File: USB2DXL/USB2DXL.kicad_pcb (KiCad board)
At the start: 4 copper layers, 38 x 42 mm, 43 parts, among them J1 XT60, J2 USB_C_Receptacle_USB2.0_16P, J3 Conn_01x03, J4 Conn_01x04, J5 Conn_01x03, J6 Conn_01x04, J7 Conn_01x04, U1 CH340E, U2 ISO7741DWR, U3 78L05G-AB3-R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

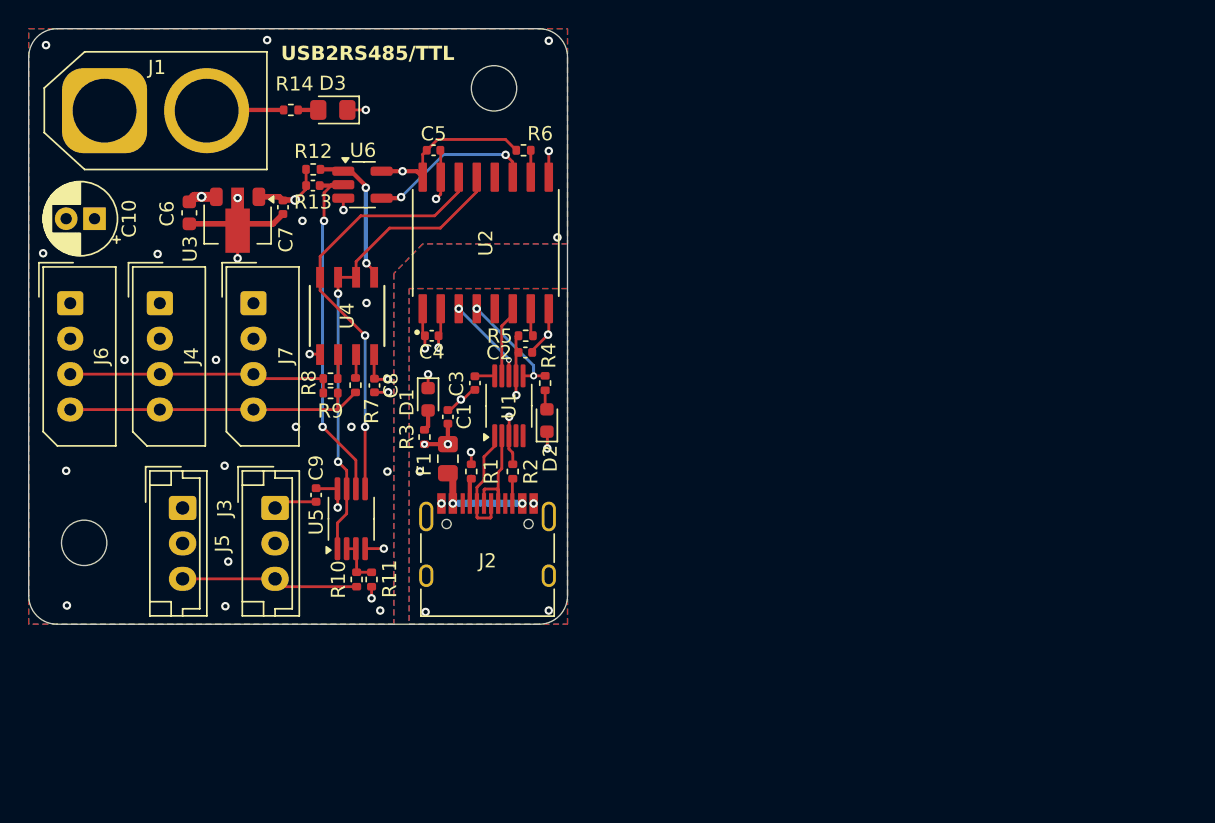
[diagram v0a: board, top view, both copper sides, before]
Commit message: マイコンからのUARTで動かせるようにした
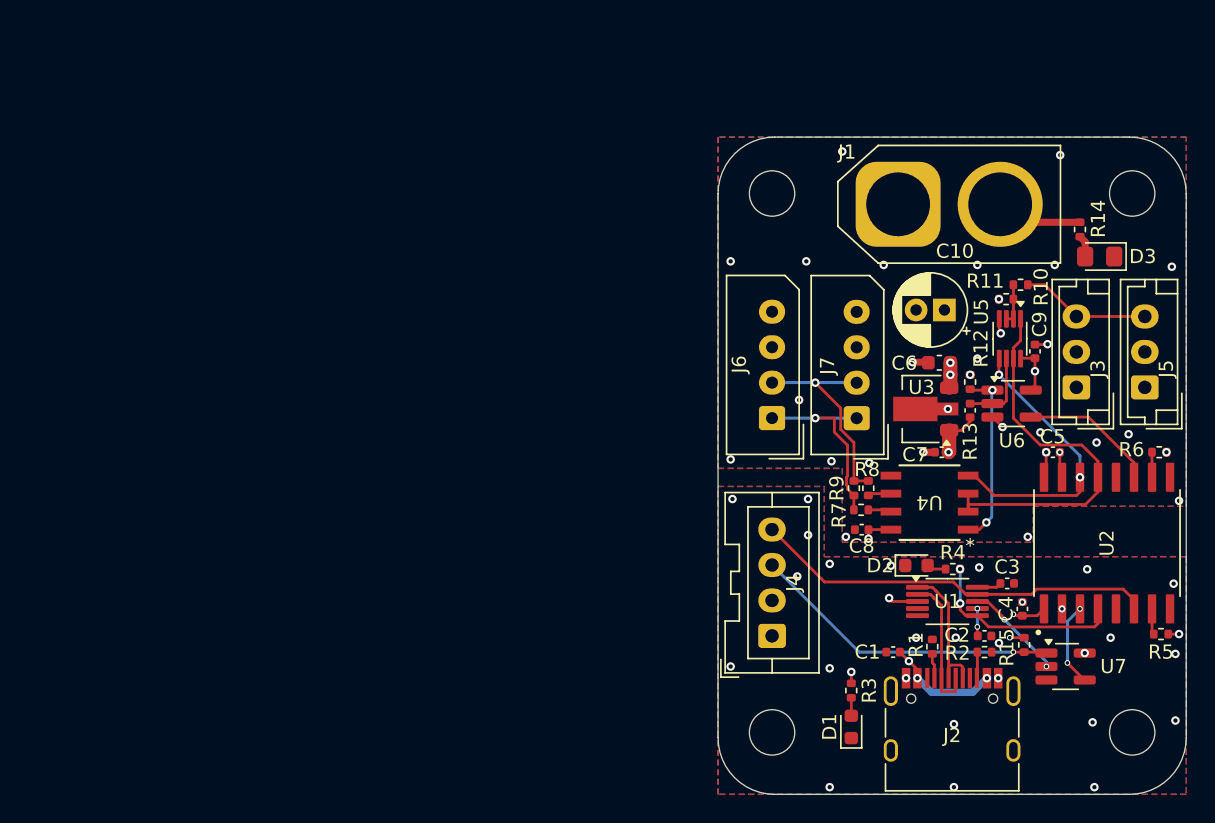
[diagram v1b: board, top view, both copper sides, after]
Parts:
- removed F1: Resettable Fuse, Fuse:Fuse_0805_2012Metric_Pad1.15x1.40mm_HandSolder
- removed the REF** at (54.4, 88.6)
- removed the REF** at (83.3, 56.6)
- added R15: 10k, Resistor_SMD:R_0402_1005Metric, F.Cu at (120.7, 95.8)
- added REF**: MountingHole_3.2mm_M3, MountingHole:MountingHole_3.2mm_M3, F.Cu at (102.9, 64.0)
- added REF**: MountingHole_3.2mm_M3, MountingHole:MountingHole_3.2mm_M3, F.Cu at (128.3, 64.0)
- added REF**: MountingHole_3.2mm_M3, MountingHole:MountingHole_3.2mm_M3, F.Cu at (102.9, 102.0)
- added REF**: MountingHole_3.2mm_M3, MountingHole:MountingHole_3.2mm_M3, F.Cu at (128.3, 102.0)
- added U7: 74AHC1G08, Package_TO_SOT_SMD:SOT-23-5_HandSoldering, F.Cu at (123.6, 97.4)
- J4: footprint Connector_Molex:Molex_SPOX_5267-04A_1x04_P2.50mm_Vertical -> Connector_JST:JST_XA_B04B-XASK-1_1x04_P2.50mm_Vertical
- R4: value 470 -> 1k
- U5: footprint Package_SO:MSOP-8_3x3mm_P0.65mm -> Package_SO:VSSOP-8_2.3x2mm_P0.5mm
- moved J5 68.4 mm to (129.2, 77.7), turned to 90 degrees
- moved C10 60.3 mm to (115.0, 72.2)
- moved J3 57.2 mm to (124.3, 77.7), turned to 90 degrees
- moved J1 56.4 mm to (111.8, 64.8)
- moved R14 56.3 mm to (124.6, 66.5), turned to -90 degrees
- moved D3 55.1 mm to (126.0, 68.5)
- moved C6 53.9 mm to (114.7, 75.9), turned to 180 degrees
- moved C9 51.7 mm to (121.4, 75.1), turned to 90 degrees
- moved R10 51.2 mm to (120.4, 70.4), turned to 0 degrees
- moved J6 50.2 mm to (102.9, 79.8), turned to 90 degrees
- moved U3 50.0 mm to (113.4, 79.2), turned to 180 degrees
- moved R6 49.6 mm to (130.2, 82.3), turned to 0 degrees
- moved C7 49.6 mm to (114.8, 82.3), turned to 180 degrees
- moved R5 49.5 mm to (130.3, 95.1), turned to 180 degrees
- moved J4 49.1 mm to (102.9, 95.2), turned to 90 degrees
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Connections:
- J2 pad A4: Net-(F1-Pad1) -> +5V
- J2 pad A6: /D- -> /D+
- J2 pad A7: /D+ -> /D-
- J2 pad A9: Net-(F1-Pad1) -> +5V
- J2 pad B4: Net-(F1-Pad1) -> +5V
- J2 pad B6: /D- -> /D+
- J2 pad B7: /D+ -> /D-
- J2 pad B9: Net-(F1-Pad1) -> +5V
- J4 pad 1: GNDPWR -> GND
- J4 pad 2: +12V -> +5V
- J4 pad 3: /A -> /TX_pin
- J4 pad 4: /B -> /RXD
- J6 pad 1: GNDPWR -> /DATA-
- J6 pad 2: +12V -> /DATA+
- J6 pad 3: /A -> +12V
- J6 pad 4: /B -> GNDPWR
- J7 pad 1: GNDPWR -> /DATA-
- J7 pad 2: +12V -> /DATA+
- J7 pad 3: /A -> +12V
- J7 pad 4: /B -> GNDPWR
- R7 pad 2: /B -> /DATA-
- R8 pad 2: /A -> /DATA+
- R9 pad 1: /A -> /DATA+
- R9 pad 2: /B -> /DATA-
- U1 pad 8: /TXD -> /TX_usb
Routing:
- net +5VP: track 23.4 -> 54.9 mm, vias 5 -> 7
- net /RXD: track 5.05 -> 28.5 mm
- net /TX_pin: track 0.00 -> 21.9 mm, vias 0 -> 1
- net /B: track 21.8 -> 0.00 mm
- net Net-(U5-Y1): track 25.2 -> 5.61 mm, vias 2 -> 0
- net /A: track 19.0 -> 0.00 mm
- net GNDPWR: track 24.8 -> 6.76 mm, vias 28 -> 26
- net /DATA+: track 0.00 -> 15.1 mm, vias 0 -> 1
- net /DATA-: track 0.00 -> 14.4 mm, vias 0 -> 1
- net GND: track 15.2 -> 2.10 mm, vias 12 -> 27
- net /TX: track 30.4 -> 20.3 mm
- net Net-(F1-Pad1): track 7.19 -> 0.00 mm, vias 2 -> 0
- net /TX_usb: track 0.00 -> 7.03 mm, vias 0 -> 2
- net /TXNOW: track 7.95 -> 14.2 mm
- net /TXEN: track 33.6 -> 27.9 mm, vias 2 -> 0
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- removed copper zone on In2.Cu, net +5VP
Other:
- board size 38 x 42 mm -> 33 x 46.4 mm
